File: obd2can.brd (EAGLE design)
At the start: 96.5 x 40.6 mm, 85 parts, among them IC1 LM339PWR, IC2 SCANTOOL, Q1 BSS138, Q2 MMBT2222, Q3 ZXMP6A13FTA, Q4 BSS138, Q5 MMBT2222, Q6 MMBT2222, Q7 8MHz, SW1 6X3.5_TACT, U1 V_REG_317SMD, U2 SN65HVD235DR, U3 MCP1700-5.0, U4 STM32F072-LQFP48, U8 MCP1700-3.3, X1 RJ45_RIGHT_ANGLEMOLEX_95001-2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, X2 RJ45_RIGHT_ANGLEMOLEX_95001-2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, Y1 16MHz

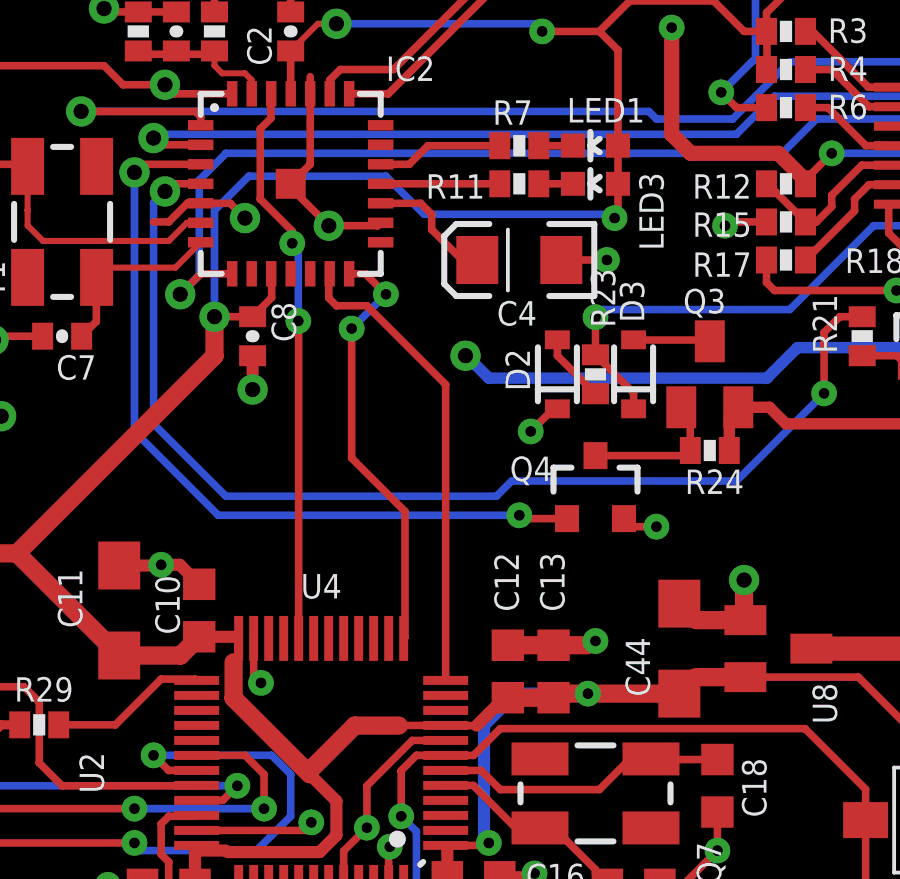
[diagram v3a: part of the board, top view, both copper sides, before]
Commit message: add NVM_RST line between STM32 and STN chips
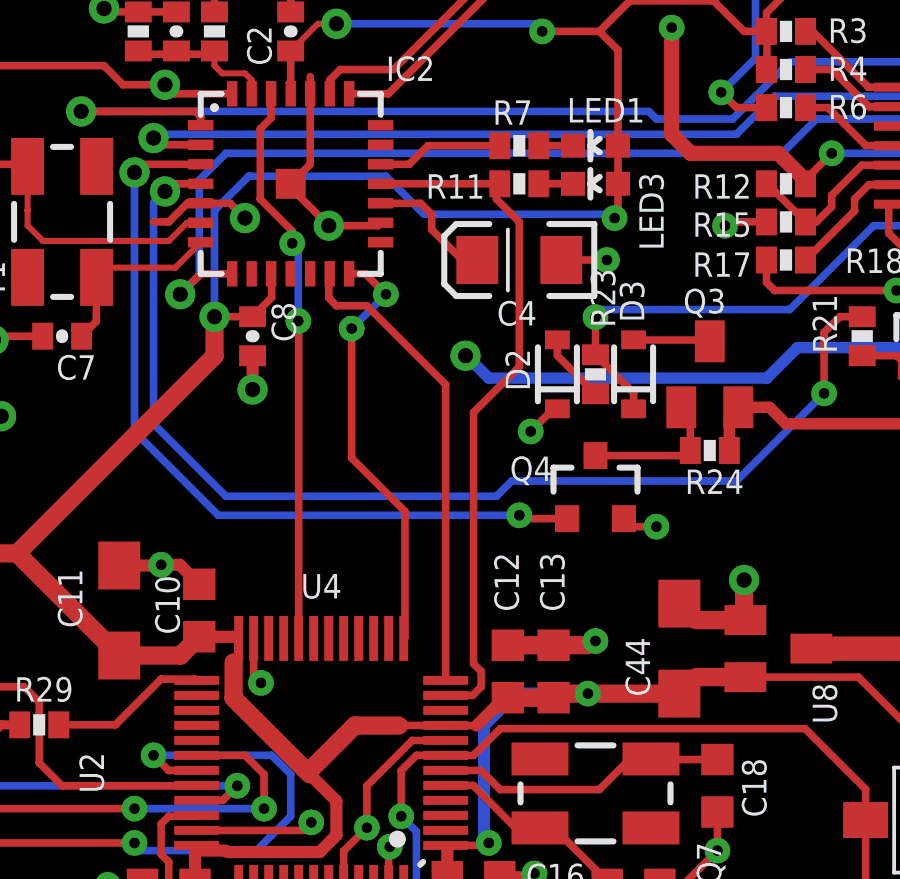
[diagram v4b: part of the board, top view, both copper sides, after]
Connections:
- net RST_NVM: now also U4.11
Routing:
- net RST_NVM: track 3.98 -> 23.1 mm
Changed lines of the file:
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@@
 <contactref element="R11" pad="2"/>
 <wire x1="38.481" y1="30.48" x2="38.466" y2="30.48" width="0.254" layer="1"/>
-<wire x1="34.496" y1="30.48" x2="38.466" y2="30.48" width="0.254" layer="1"/>
+<wire x1="38.354" y1="30.48" x2="38.466" y2="30.48" width="0.254" layer="1"/>
+<wire x1="34.496" y1="30.48" x2="38.354" y2="30.48" width="0.254" layer="1"/>
+<wire x1="38.354" y1="30.48" x2="38.354" y2="29.972" width="0.254" layer="1"/>
+<wire x1="38.354" y1="29.972" x2="39.116" y2="29.21" width="0.254" layer="1"/>
+<wire x1="39.116" y1="29.21" x2="39.116" y2="24.384" width="0.254" layer="1"/>
+<wire x1="39.116" y1="24.384" x2="37.592" y2="22.86" width="0.254" layer="1"/>
+<contactref element="U4" pad="11"/>
+<wire x1="37.592" y1="22.86" x2="37.592" y2="14.478" width="0.254" layer="1"/>
+<wire x1="37.592" y1="14.478" x2="37.846" y2="14.224" width="0.254" layer="1"/>
+<wire x1="36.662" y1="13.426" x2="37.556" y2="13.426" width="0.254" layer="1"/>
+<wire x1="37.556" y1="13.426" x2="37.846" y2="13.716" width="0.254" layer="1"/>
+<wire x1="37.846" y1="13.716" x2="37.846" y2="14.224" width="0.254" layer="1"/>
 </signal>
 <signal name="N$30">
